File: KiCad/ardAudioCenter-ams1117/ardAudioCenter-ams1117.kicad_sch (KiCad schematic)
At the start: 29 parts, among them J1 2-pin_power_input_header, J2 AudioPlug3, J3 4-pin_I2C_LCD_header, U1 2-pole_power_in_screw_terminal, U10 CD4052B, U11 MCP41010, U12 4-pole_RL-input_screw_terminal, U13 4-pole_RL-input_screw_terminal, U14 4-pole_RL-input_screw_terminal, U15 TEA5767_FM_Radio_Module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

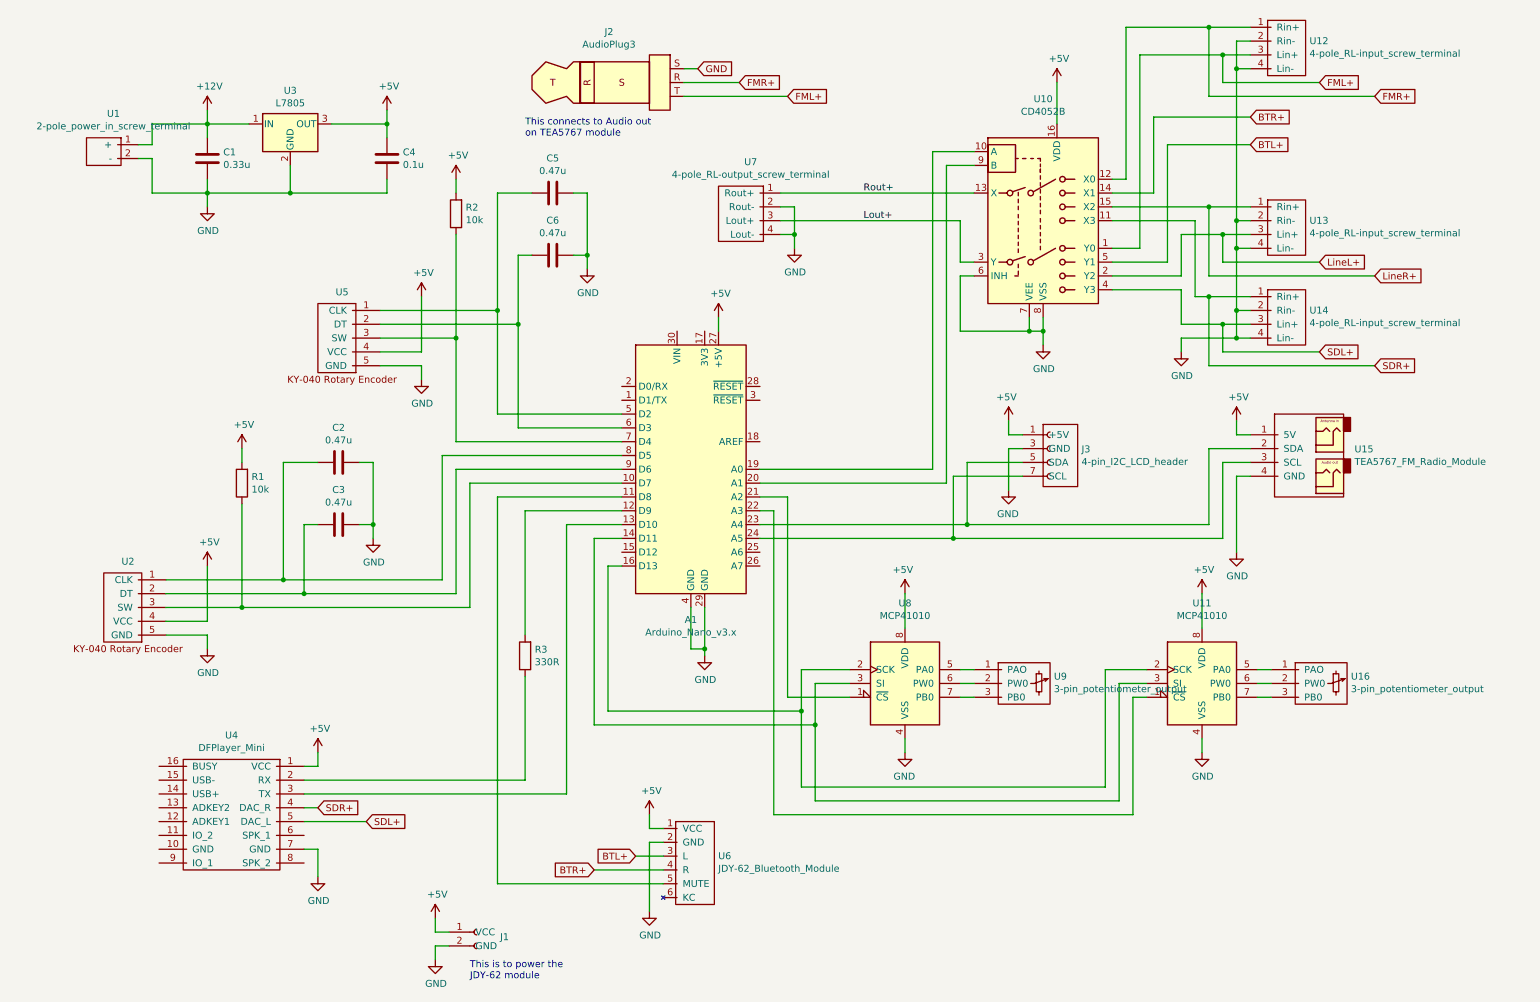
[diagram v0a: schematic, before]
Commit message: pcb, moved to pio
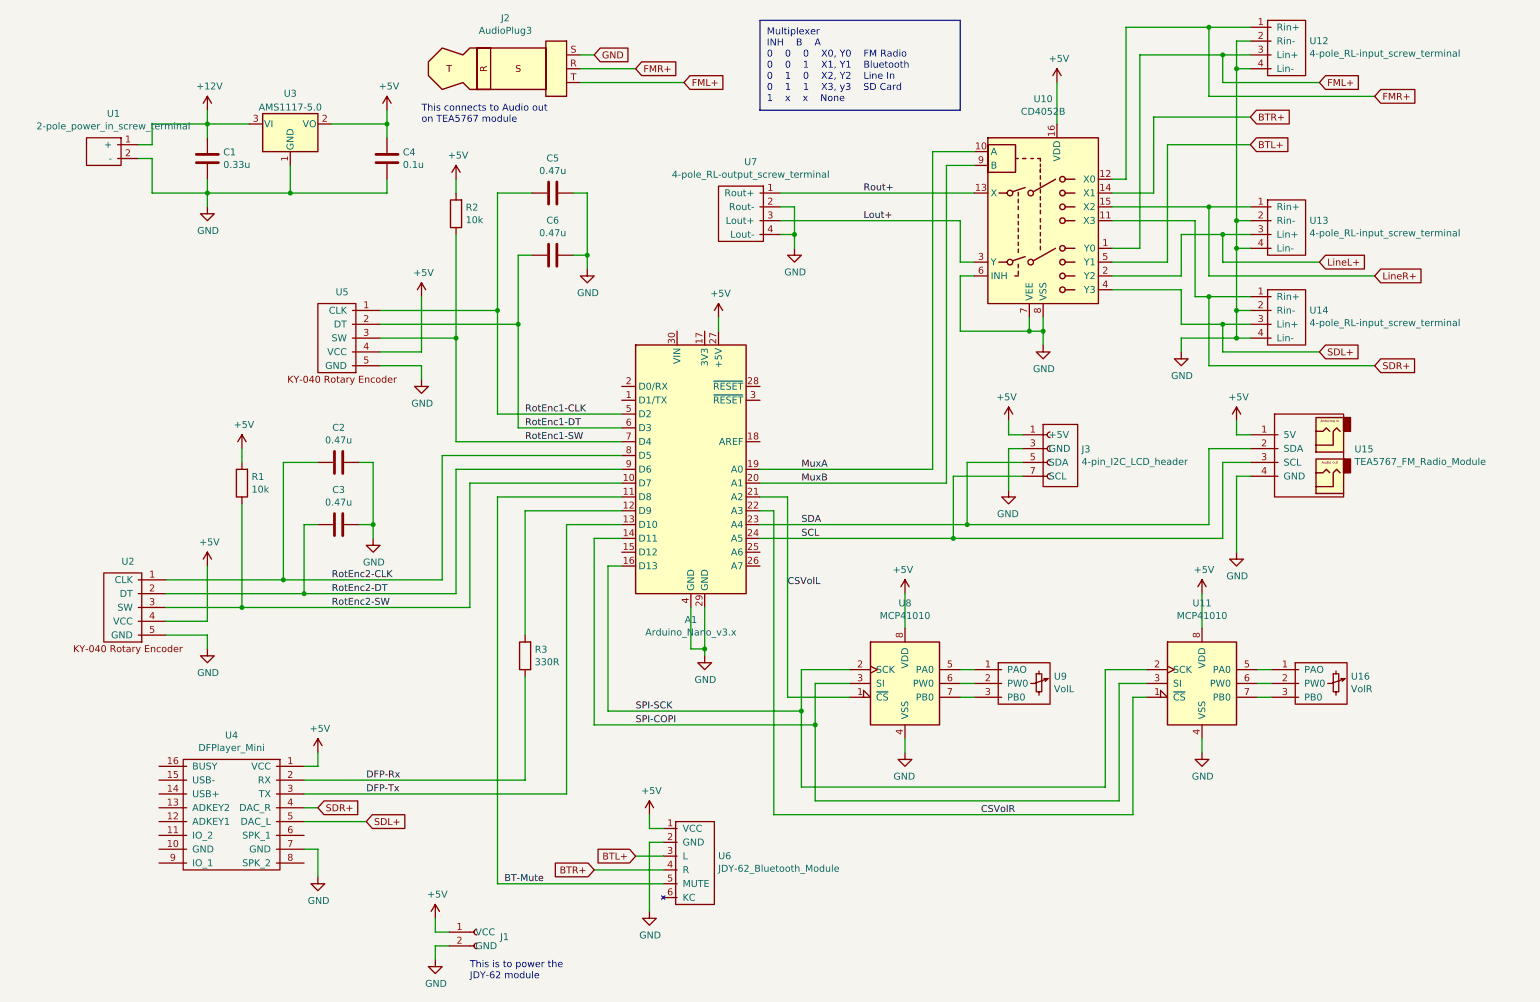
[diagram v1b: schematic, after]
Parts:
- removed U3: L7805, My_Misc:TO-220-3_Vertical_larger, symbol Regulator_Linear:L7805
- added U3: AMS1117-5.0, Package_TO_SOT_SMD:SOT-223-3_TabPin2, symbol Regulator_Linear:AMS1117-5.0
- A1: footprint (none) -> My_Arduino:Arduino_Nano_WithMountingHoles_larger
- U16: value 3-pin_potentiometer_output -> VolR
- U9: value 3-pin_potentiometer_output -> VolL
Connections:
- net +12V: now also U3.3 (VI)
- net +5V: now also U3.2 (VO)
- net GND: now also U3.1 (GND)
- net MuxA: now reaches A1.19 (A0), U10.10 (A)
- net MuxB: now reaches A1.20 (A1), U10.9 (B)
- net CSVolL: now reaches A1.21 (A2), U8.1 (~{CS})
- net SPI-SCK: now reaches A1.16 (D13), U11.2 (SCK), U8.2 (SCK)
- net SPI-COPI: now reaches A1.14 (D11), U11.3 (SI), U8.3 (SI)
- net CSVolR: now reaches A1.22 (A3), U11.1 (~{CS})
- net SDA: now reaches A1.23 (A4), J3.5 (SDA), U15.2 (SDA)
- net SCL: now reaches A1.24 (A5), J3.7 (SCL), U15.3 (SCL)
- net RotEnc1-CLK: now reaches A1.5 (D2), C5.1, U5.1 (CLK)
- net RotEnc1-DT: now reaches A1.6 (D3), C6.2, U5.2 (DT)
- net RotEnc1-SW: now reaches A1.7 (D4), R2.1, U5.3 (SW)
- net RotEnc2-CLK: now reaches A1.8 (D5), C2.1, U2.1 (CLK)
- net RotEnc2-DT: now reaches A1.9 (D6), C3.2, U2.2 (DT)
- net RotEnc2-SW: now reaches A1.10 (D7), R1.1, U2.3 (SW)
- net BT-Mute: now reaches A1.11 (D8), U6.5 (MUTE)
- net DFP-Tx: now reaches A1.13 (D10), U4.3 (TX)
- net DFP-Rx: now reaches R3.1, U4.2 (RX)
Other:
- note added: "Multiplexer INH B A 0 0 0 X0, Y0 FM Radio 0 0 1 X1, Y1 Bluetooth 0 1 0 X2, Y2 Line In 0 1 1 X3, y3 SD Card 1 x x None"
- moved on the sheet: J2
